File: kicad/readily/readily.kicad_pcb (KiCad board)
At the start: 2 copper layers, 63.5 x 55.9 mm, 33 parts, among them J1 Conn_01x09_Socket, J3 USB_C_Receptacle_USB2.0_16P, J4 Conn_01x03, SW2 SW_SPST, SW3 SW_SPST, U1 ESP32-S3-WROOM-1, U2 BQ24040DSQR, U3 TPD2EUSB30, U4 TLV75533PDRV

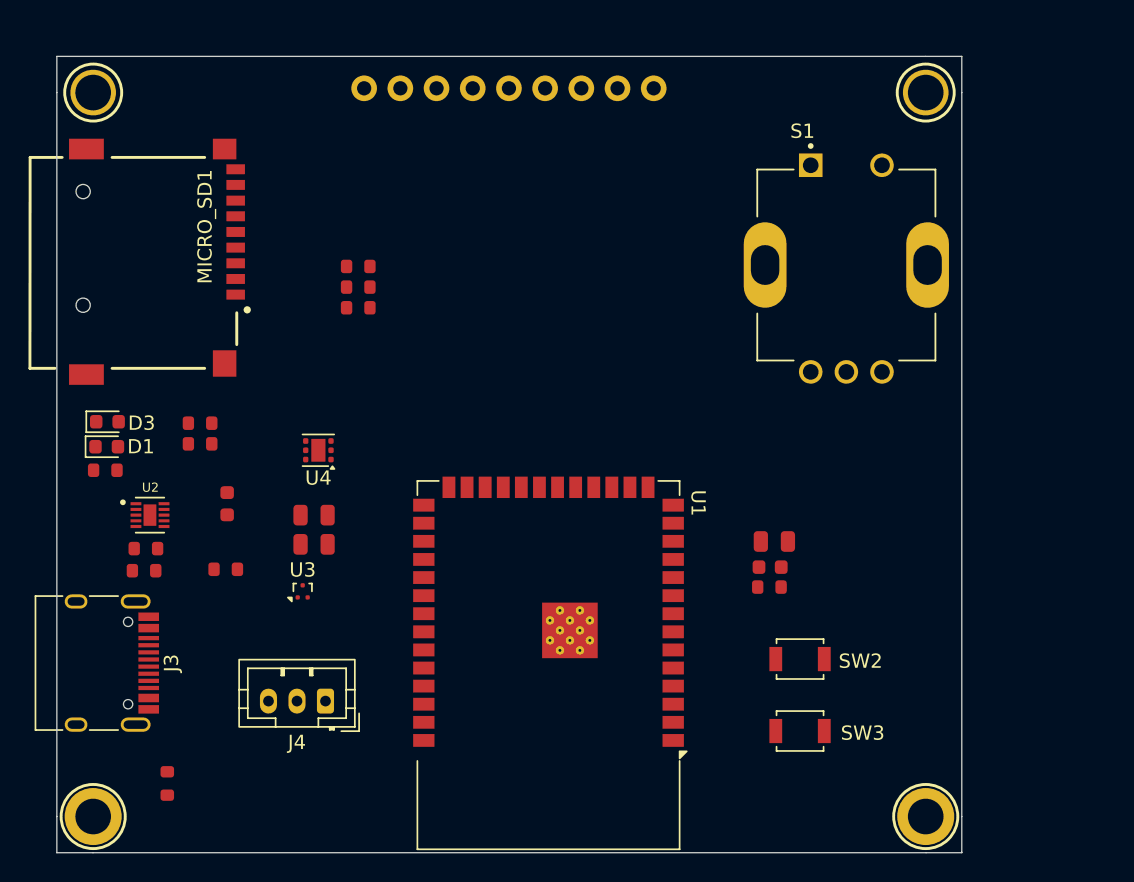
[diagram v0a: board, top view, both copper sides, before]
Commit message: fix: cleared out all DRC errors
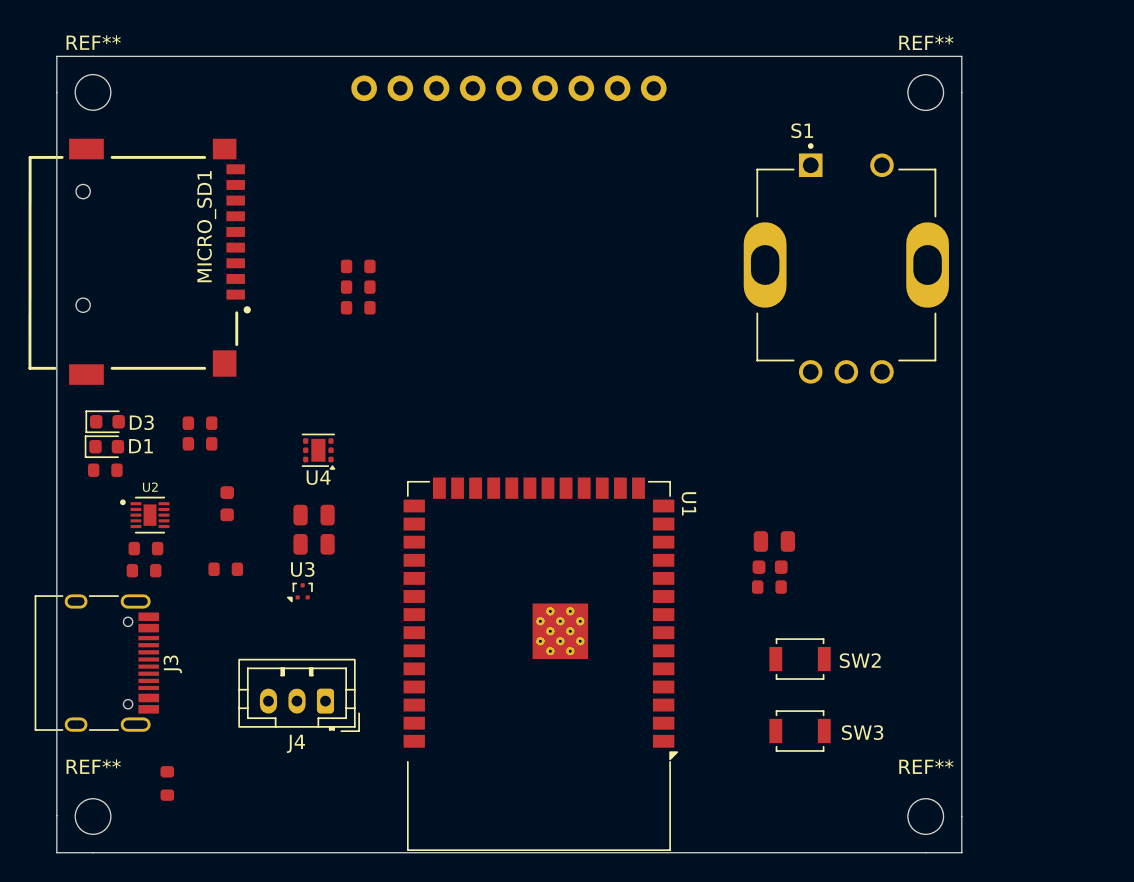
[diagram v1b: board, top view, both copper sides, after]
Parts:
- removed U$21, U$22: MOUNTINGHOLE2.5_THICK, display:MOUNTINGHOLE_2.5_PLATED_THICK
- removed U$27, U$28: MOUNTINGHOLE2.5, display:MOUNTINGHOLE_2.5_PLATED
- added REF**: MountingHole_2.5mm, MountingHole:MountingHole_2.5mm, F.Cu at (210.9, 52.3)
- added REF**: MountingHole_2.5mm, MountingHole:MountingHole_2.5mm, F.Cu at (152.4, 52.3)
- added REF**: MountingHole_2.5mm, MountingHole:MountingHole_2.5mm, F.Cu at (152.4, 103.1)
- added REF**: MountingHole_2.5mm, MountingHole:MountingHole_2.5mm, F.Cu at (210.9, 103.1)
- moved U1 0.67 mm to (183.7, 92.6)

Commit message: feat: adding vias and tracks to all components
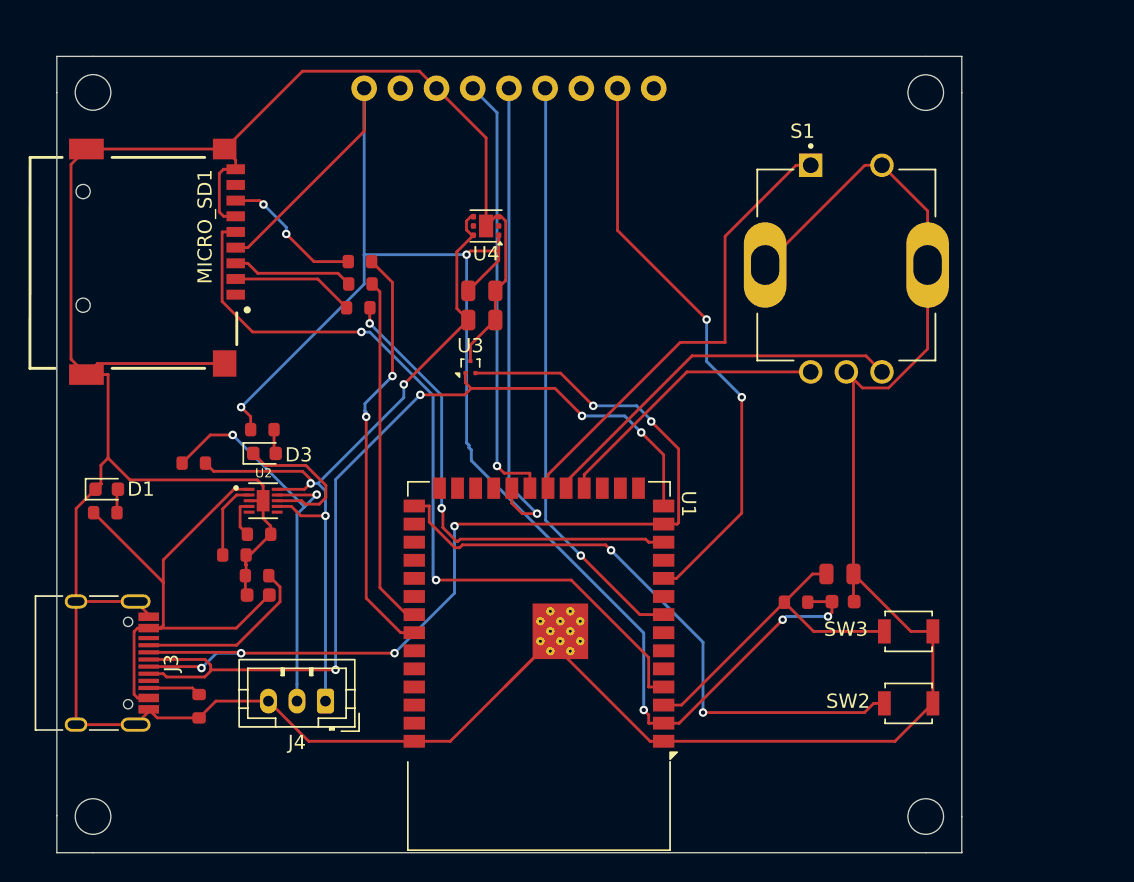
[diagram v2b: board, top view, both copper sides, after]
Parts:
- moved C3 19.7 mm to (179.7, 66.2)
- moved U4 19.7 mm to (180.0, 61.7)
- moved C2 19.7 mm to (179.7, 68.3)
- moved U3 19.7 mm to (178.9, 71.6)
- moved D3 11.2 mm to (164.5, 77.6)
- moved SW3 10.3 mm to (209.7, 90.1), turned to 180 degrees
- moved SW2 8.23 mm to (209.7, 95.2), turned to 180 degrees
- moved U2 8.00 mm to (164.4, 80.9)
- moved R7 8.00 mm to (164.1, 83.3), turned to 180 degrees
- moved C1 6.77 mm to (164.0, 87.6), turned to 180 degrees
- moved R6 6.43 mm to (162.4, 84.8), turned to 180 degrees
- moved R5 5.86 mm to (159.9, 95.4), turned to -90 degrees
- moved C4 5.66 mm to (205.1, 88.0), turned to 0 degrees
- moved C5 5.13 mm to (204.8, 86.1)
- moved R12 4.39 mm to (164.3, 76.0)
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- renumbered REF** to Mount1, REF** to Mount2, REF** to Mount3, REF** to Mount4
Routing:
- net GND: track 0.00 -> 288.3 mm
- net +3V3: track 0.00 -> 115.4 mm, vias 0 -> 5
- net D-: track 0.00 -> 73.2 mm, vias 0 -> 6
- net D+: track 0.00 -> 64.1 mm, vias 0 -> 4
- net SD_CLK: track 0.00 -> 56.7 mm, vias 0 -> 2
- net SYS_OUT: track 0.00 -> 55.3 mm, vias 0 -> 3
- net GPIO0: track 0.00 -> 43.9 mm, vias 0 -> 2
- net DISP_CS: track 0.00 -> 41.4 mm, vias 0 -> 1
- net DISP_DISP: track 0.00 -> 41.0 mm, vias 0 -> 2
- net +5V: track 0.00 -> 36.8 mm
- net SD_CS: track 0.00 -> 34.1 mm, vias 0 -> 2
- net DISP_DI: track 0.00 -> 33.8 mm, vias 0 -> 1
- net RT_SW: track 0.00 -> 32.7 mm
- net DISP_CLK: track 0.00 -> 30.8 mm, vias 0 -> 1
- net SD_MISO: track 0.00 -> 30.0 mm, vias 0 -> 2
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
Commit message: feat: updating the specs with the final rotatory encoder switch
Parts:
- removed S1: PEC11R-4220F-S0024, RotatoryEncoder:XDCR_PEC11R-4220F-S0024
- added U5: ED08905M-FE15C7_0-C10-2053, JLCPCB Import:ED08905M-FE15C7_0-C10-2053, F.Cu at (204.3, 63.0)
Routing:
- net GND: track 288.3 -> 272.8 mm
- net RT_CLK: track 19.8 -> 32.7 mm
- net RT_SW: track 32.7 -> 36.6 mm
- net RT_DT: track 26.7 -> 25.4 mm, vias 0 -> 2

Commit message: feat: version 1.0 of the pcb
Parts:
- removed J4: Conn_01x03, Connector_JST:JST_PH_B3B-PH-K_1x03_P2.00mm_Vertical
- added U6: WAFER-PH2_0-3PWB, JLCImport:WAFER-PH2_0-3PWB, F.Cu at (168.2, 94.4)
- C1: value 4.7uF -> 4.7uF 0603
- C2, C3, C5: value 10uF -> 10uF 0805
- C4: value 100n -> 100nF 0603
- D1: value LED -> White 0603
- D3: value LED -> LED 0603
- R10, R9: value 5.1K -> 5.1KΩ 0603
- R11, R13, R14, R7, R8: value 10kΩ -> 10kΩ 0603
- R12: value 2.2K -> 2.2KΩ 0603
- R4, R5: value 5.1kΩ -> 5.1kΩ 0603
- R6: value 1kΩ -> 1kΩ 0603
- SW2, SW3: footprint Button_Switch_SMD:SW_SPST_B3U-1000P -> JLCImport:TS-1088-AR02016
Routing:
- net GND: track 272.8 -> 278.8 mm
- net BAT_NTC: track 29.5 -> 26.6 mm, vias 2 -> 3
- net SYS_OUT: track 55.3 -> 53.2 mm
- net D+: track 64.1 -> 62.1 mm
- net D-: vias 6 -> 5
